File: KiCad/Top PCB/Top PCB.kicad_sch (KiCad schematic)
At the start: 44 parts, among them SW1 SW_MEC_5G, U1 SeeeduinoXIAO

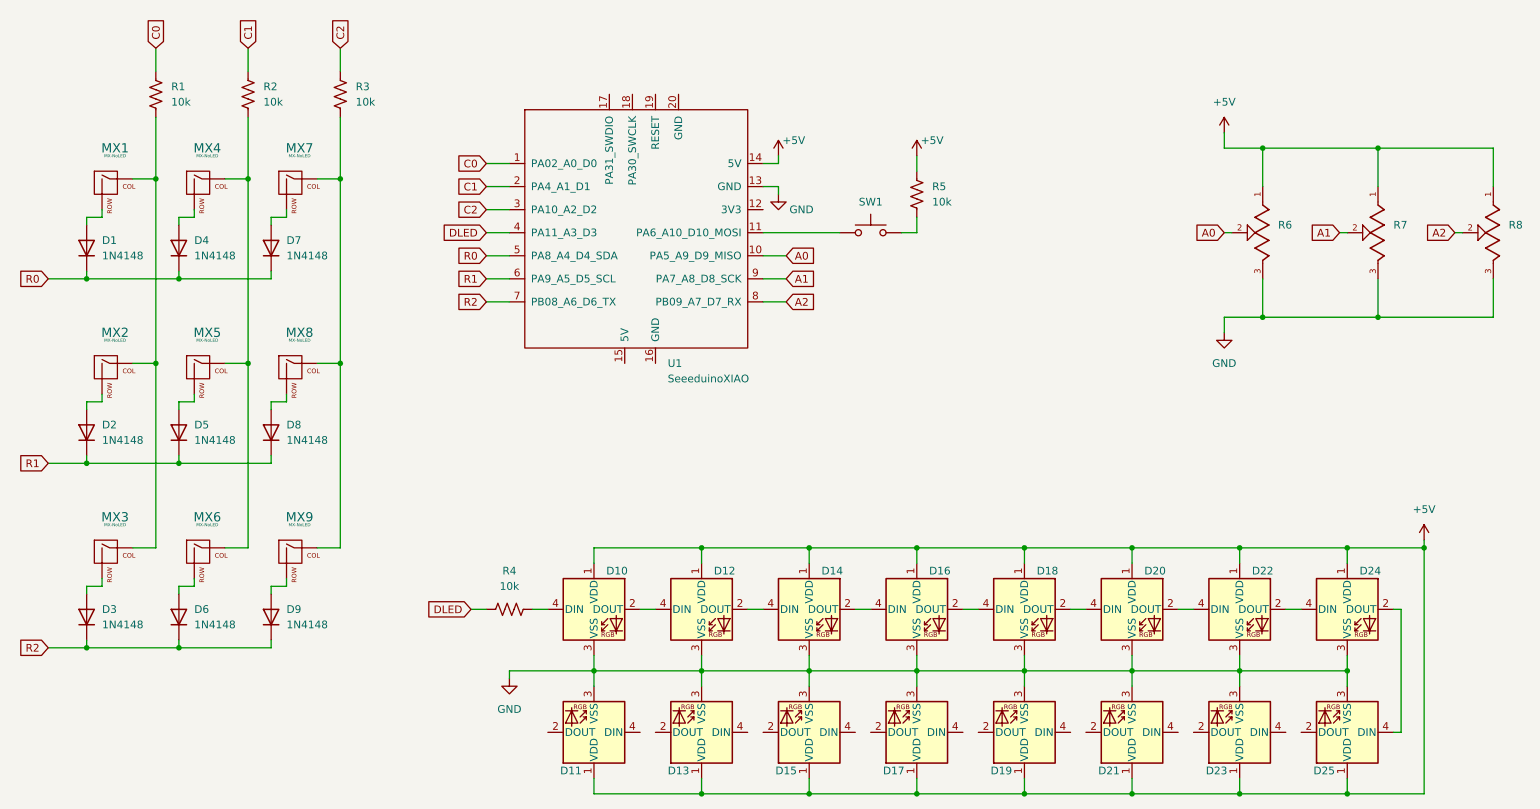
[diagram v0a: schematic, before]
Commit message: Split PCB into top, bottom. Develop Top
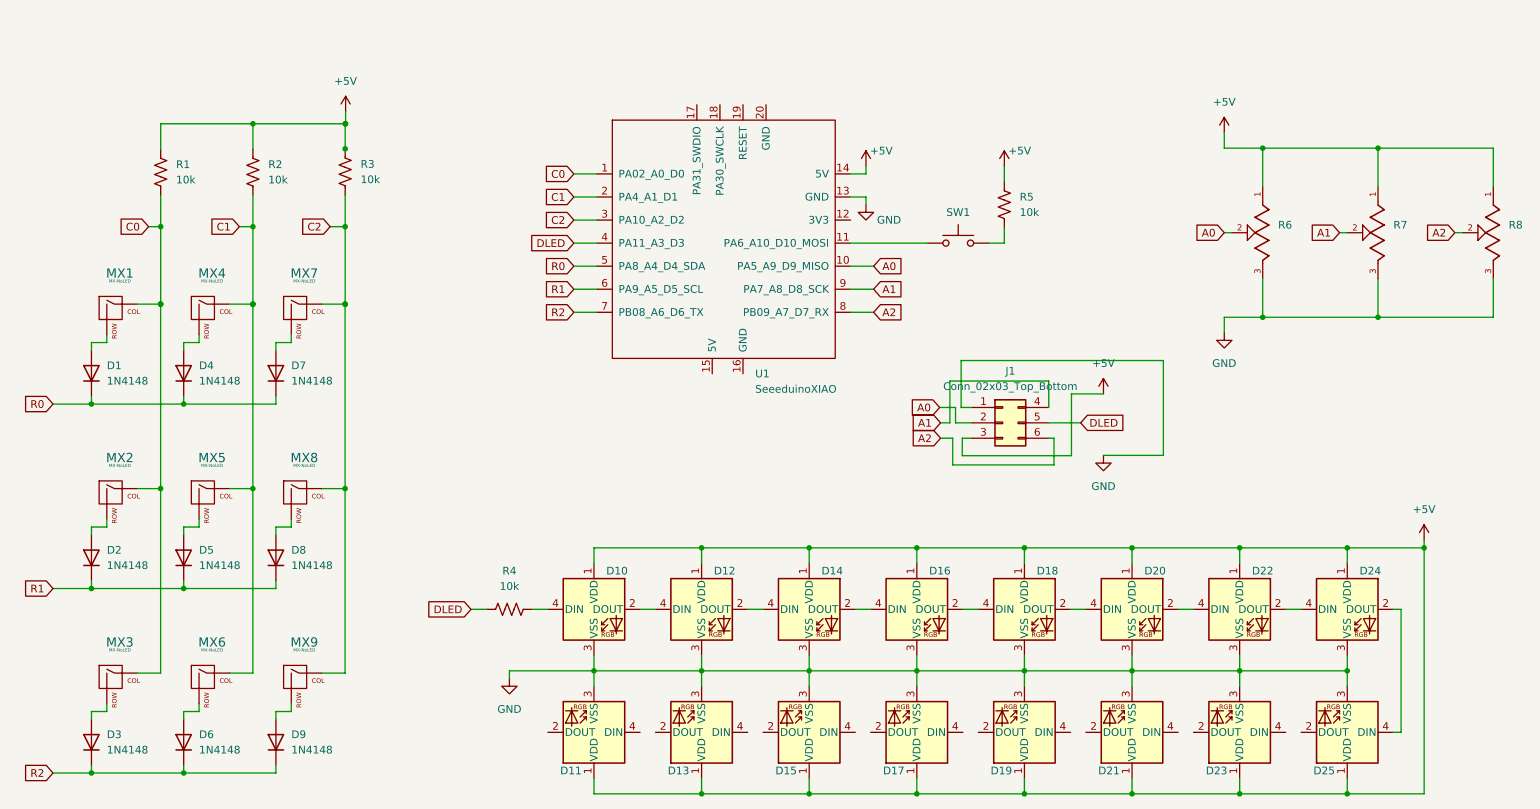
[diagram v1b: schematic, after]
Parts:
- added J1: Conn_02x03_Top_Bottom, Connector_PinHeader_2.54mm:PinHeader_2x03_P2.54mm_Vertical, symbol Connector_Generic:Conn_02x03_Top_Bottom
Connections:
- net +5V: now also R1.1, R2.1, R3.2, J1.3 (Pin_3)
- net A0: now also J1.2 (Pin_2)
- net A1: now also J1.4 (Pin_4)
- net A2: now also J1.6 (Pin_6)
- net C0: now also MX1.1 (COL), MX2.1 (COL), MX3.1 (COL), R1.2; no longer R1.1
- net C1: now also MX4.1 (COL), MX5.1 (COL), MX6.1 (COL), R2.2; no longer R2.1
- net C2: now also MX7.1 (COL), MX8.1 (COL), MX9.1 (COL)
- net DLED: now also J1.5 (Pin_5)
- net GND: now also J1.1 (Pin_1)
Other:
- moved on the sheet: D1, D2, D3, D4, D5, D6, D7, D8, D9, MX1, MX2, MX3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

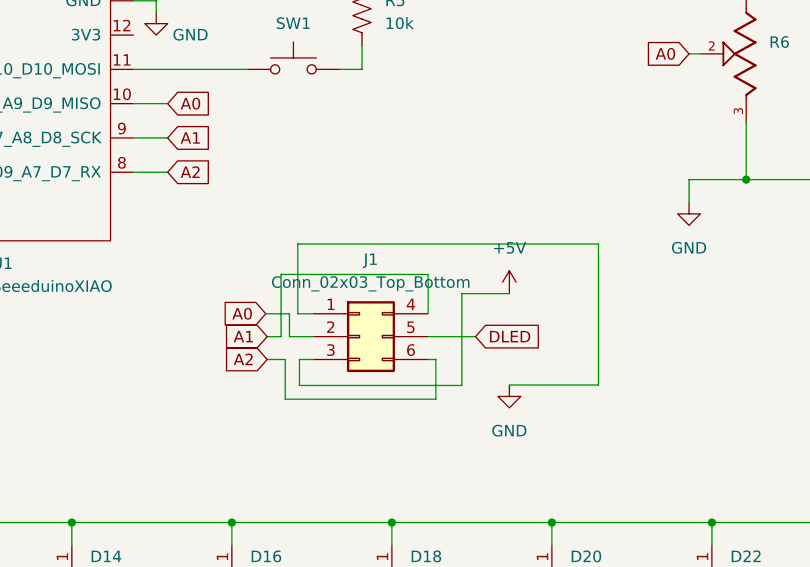
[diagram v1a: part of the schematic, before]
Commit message: Restructuring PCBs to only one top PCB, handwired switches
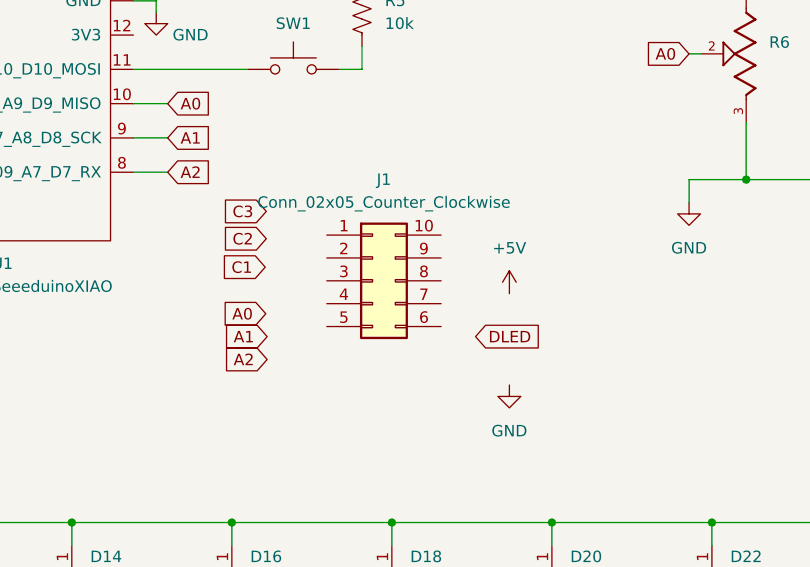
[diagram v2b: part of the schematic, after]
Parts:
- removed J1: Conn_02x03_Top_Bottom, Connector_PinHeader_2.54mm:PinHeader_2x03_P2.54mm_Vertical, symbol Connector_Generic:Conn_02x03_Top_Bottom
- added J1: Conn_02x05_Counter_Clockwise, Connector_PinHeader_2.54mm:PinHeader_2x05_P2.54mm_Vertical, symbol Connector_Generic:Conn_02x05_Counter_Clockwise
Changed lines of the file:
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@@
-    (stroke (width 0) (type default) (color 0 0 0 0))
-  )
-  (wire (pts (xy 178.6527 93.645) (xy 176.6431 93.645))
-    (stroke (width 0) (type default) (color 0 0 0 0))
-  )
-  (wire (pts (xy 213.4552 96.4802) (xy 213.4552 80.8131))
     (stroke (width 0) (type default) (color 0 0 0 0))
   )
@@
     (stroke (width 0) (type default) (color 0 0 0 0))
   )
-  (wire (pts (xy 194.5248 88.565) (xy 194.5248 84.1974))
-    (stroke (width 0) (type default) (color 0 0 0 0))
-  )
   (wire (pts (xy 226.06 132.08) (xy 226.06 134.62))
     (stroke (width 0) (type default) (color 0 0 0 0))
@@
     (stroke (width 0) (type default) (color 0 0 0 0))
   )
-  (wire (pts (xy 178.6527 98.0589) (xy 178.6527 93.645))
-    (stroke (width 0) (type default) (color 0 0 0 0))
-  )
   (wire (pts (xy 51.59 118.48) (xy 51.59 117.21))
     (stroke (width 0) (type default) (color 0 0 0 0))
@@
     (stroke (width 0) (type default) (color 0 0 0 0))
   )
-  (wire (pts (xy 203.5567 86.3311) (xy 198.2693 86.3311))
-    (stroke (width 0) (type default) (color 0 0 0 0))
-  )
   (wire (pts (xy 66.83 118.48) (xy 51.59 118.48))
     (stroke (width 0) (type default) (color 0 0 0 0))
@@
     (stroke (width 0) (type default) (color 0 0 0 0))
   )
-  (wire (pts (xy 203.5567 96.4802) (xy 213.4552 96.4802))
-    (stroke (width 0) (type default) (color 0 0 0 0))
-  )
-  (wire (pts (xy 195.3886 98.0589) (xy 178.6527 98.0589))
-    (stroke (width 0) (type default) (color 0 0 0 0))
-  )
   (wire (pts (xy 223.52 73.66) (xy 229.87 73.66))
     (stroke (width 0) (type default) (color 0 0 0 0))
@@
     (stroke (width 0) (type default) (color 0 0 0 0))
   )
-  (wire (pts (xy 194.5248 84.1974) (xy 178.1891 84.1974))
-    (stroke (width 0) (type default) (color 0 0 0 0))
-  )
-  (wire (pts (xy 195.3886 93.645) (xy 195.3886 98.0589))
-    (stroke (width 0) (type default) (color 0 0 0 0))
-  )
-  (wire (pts (xy 194.5248 91.105) (xy 199.7978 91.105))
-    (stroke (width 0) (type default) (color 0 0 0 0))
-  )
   (wire (pts (xy 208.28 132.08) (xy 226.06 132.08))
     (stroke (width 0) (type default) (color 0 0 0 0))
@@
     (stroke (width 0) (type default) (color 0 0 0 0))
   )
-  (wire (pts (xy 213.4552 80.8131) (xy 180.0435 80.8131))
-    (stroke (width 0) (type default) (color 0 0 0 0))
-  )
   (wire (pts (xy 119.38 152.4) (xy 137.16 152.4))
     (stroke (width 0) (type default) (color 0 0 0 0))
@@
     (stroke (width 0) (type default) (color 0 0 0 0))
   )
-  (wire (pts (xy 176.4927 88.565) (xy 179.1213 88.565))
-    (stroke (width 0) (type default) (color 0 0 0 0))
-  )
   (wire (pts (xy 51.59 148.96) (xy 36.35 148.96))
     (stroke (width 0) (type default) (color 0 0 0 0))
@@
     (stroke (width 0) (type default) (color 0 0 0 0))
   )
-  (wire (pts (xy 181.8248 88.565) (xy 180.0435 88.565))
-    (stroke (width 0) (type default) (color 0 0 0 0))
-  )
   (wire (pts (xy 187.18 48.71) (xy 187.18 51.25))
     (stroke (width 0) (type default) (color 0 0 0 0))
@@
     (stroke (width 0) (type default) (color 0 0 0 0))
   )
-  (wire (pts (xy 178.1891 84.1974) (xy 178.1891 91.105))
-    (stroke (width 0) (type default) (color 0 0 0 0))
-  )
   (wire (pts (xy 229.87 67.31) (xy 229.87 73.66))
     (stroke (width 0) (type default) (color 0 0 0 0))
   )
-  (wire (pts (xy 194.5248 93.645) (xy 195.3886 93.645))
-    (stroke (width 0) (type default) (color 0 0 0 0))
-  )
   (wire (pts (xy 45.79 58.69) (xy 47.79 58.69))
     (stroke (width 0) (type default) (color 0 0 0 0))
@@
     (stroke (width 0) (type default) (color 0 0 0 0))
   )
-  (wire (pts (xy 180.0435 88.565) (xy 180.0435 80.8131))
-    (stroke (width 0) (type default) (color 0 0 0 0))
-  )
   (wire (pts (xy 30 88) (xy 36.35 88))
     (stroke (width 0) (type default) (color 0 0 0 0))
@@
     (stroke (width 0) (type default) (color 0 0 0 0))
   )
-  (wire (pts (xy 198.2693 96.529) (xy 180.229 96.529))
-    (stroke (width 0) (type default) (color 0 0 0 0))
-  )
   (wire (pts (xy 59.21 132.45) (xy 63.02 132.45))
     (stroke (width 0) (type default) (color 0 0 0 0))
@@
     (stroke (width 0) (type default) (color 0 0 0 0))
   )
-  (wire (pts (xy 179.1213 88.565) (xy 179.1213 91.105))
-    (stroke (width 0) (type default) (color 0 0 0 0))
-  )
   (wire (pts (xy 78.27 41.69) (xy 63.03 41.69))
     (stroke (width 0) (type default) (color 0 0 0 0))
@@
     (stroke (width 0) (type default) (color 0 0 0 0))
   )
-  (wire (pts (xy 181.8248 93.645) (xy 180.229 93.645))
-    (stroke (width 0) (type default) (color 0 0 0 0))
-  )
-  (wire (pts (xy 178.1891 91.105) (xy 176.6431 91.105))
-    (stroke (width 0) (type default) (color 0 0 0 0))
-  )
   (wire (pts (xy 105.41 132.08) (xy 105.41 133.35))
     (stroke (width 0) (type default) (color 0 0 0 0))
@@
     (stroke (width 0) (type default) (color 0 0 0 0))
   )
-  (wire (pts (xy 180.229 93.645) (xy 180.229 96.529))
-    (stroke (width 0) (type default) (color 0 0 0 0))
-  )
   (wire (pts (xy 172.72 111.76) (xy 190.5 111.76))
     (stroke (width 0) (type default) (color 0 0 0 0))
@@
     (stroke (width 0) (type default) (color 0 0 0 0))
   )
-  (wire (pts (xy 198.2693 86.3311) (xy 198.2693 96.529))
-    (stroke (width 0) (type default) (color 0 0 0 0))
-  )
   (wire (pts (xy 51.59 88) (xy 51.59 86.73))
-    (stroke (width 0) (type default) (color 0 0 0 0))
-  )
-  (wire (pts (xy 179.1213 91.105) (xy 181.8248 91.105))
     (stroke (width 0) (type default) (color 0 0 0 0))
   )
@@
     )
   )
+  (global_label "C1" (shape input) (at 176.4301 83.3848 180) (fields_autoplaced)
+    (effects (font (size 1.27 1.27)) (justify right))
+    (property "Intersheet References" "${INTERSHEET_REFS}" (id 0) (at 171.5375 83.3054 0)
+      (effects (font (size 1.27 1.27)) (justify right) hide)
+    )
+  )
   (global_label "DLED" (shape input) (at 199.7978 91.105 0) (fields_autoplaced)
     (effects (font (size 1.27 1.27)) (justify left))
@@
     )
   )
+  (global_label "C2" (shape input) (at 176.547 80.2297 180) (fields_autoplaced)
+    (effects (font (size 1.27 1.27)) (justify right))
+    (property "Intersheet References" "${INTERSHEET_REFS}" (id 0) (at 171.6544 80.1503 0)
+      (effects (font (size 1.27 1.27)) (justify right) hide)
+    )
+  )
   (global_label "A2" (shape input) (at 261.62 59.69 180) (fields_autoplaced)
     (effects (font (size 1.27 1.27)) (justify right))
@@
     (effects (font (size 1.27 1.27)) (justify right))
     (property "Intersheet References" "${INTERSHEET_REFS}" (id 0) (at 171.9319 91.0256 0)
+      (effects (font (size 1.27 1.27)) (justify right) hide)
+    )
+  )
+  (global_label "C3" (shape input) (at 176.547 77.1914 180) (fields_autoplaced)
+    (effects (font (size 1.27 1.27)) (justify right))
+    (property "Intersheet References" "${INTERSHEET_REFS}" (id 0) (at 171.6544 77.112 0)
       (effects (font (size 1.27 1.27)) (justify right) hide)
     )
@@
     (pin "9")
   )
+  (symbol (lib_id "Connector_Generic:Conn_02x05_Counter_Clockwise") (at 188.3496 84.904 0) (unit 1)
+    (in_bom yes) (on_board yes) (fields_autoplaced)
+    (property "Reference" "J1" (id 0) (at 189.6196 73.66 0))
+    (property "Value" "Conn_02x05_Counter_Clockwise" (id 1) (at 189.6196 76.2 0))
+    (property "Footprint" "Connector_PinHeader_2.54mm:PinHeader_2x05_P2.54mm_Vertical" (id 2) (at 188.3496 84.904 0)
+      (effects (font (size 1.27 1.27)) hide)
+    )
+    (property "Datasheet" "~" (id 3) (at 188.3496 84.904 0)
+      (effects (font (size 1.27 1.27)) hide)
+    )
+    (pin "1")
+    (pin "10")
+    (pin "2")
+    (pin "3")
+    (pin "4")
+    (pin "5")
+    (pin "6")
+    (pin "7")
+    (pin "8")
+    (pin "9")
+  )
   (symbol (lib_id "Diode:1N4148") (at 36.35 143.88 90) (unit 1)
     (in_bom yes) (on_board yes) (fields_autoplaced)
@@
     (pin "2")
   )
-  (symbol (lib_id "Connector_Generic:Conn_02x03_Top_Bottom") (at 186.9048 91.105 0) (unit 1)
-    (in_bom yes) (on_board yes) (fields_autoplaced)
-    (property "Reference" "J1" (id 0) (at 188.1748 82.55 0))
-    (property "Value" "Conn_02x03_Top_Bottom" (id 1) (at 188.1748 85.09 0))
-    (property "Footprint" "Connector_PinHeader_2.54mm:PinHeader_2x03_P2.54mm_Vertical" (id 2) (at 186.9048 91.105 0)
-      (effects (font (size 1.27 1.27)) hide)
-    )
-    (property "Datasheet" "~" (id 3) (at 186.9048 91.105 0)
-      (effects (font (size 1.27 1.27)) hide)
-    )
-    (pin "1")
-    (pin "2")
-    (pin "3")
-    (pin "4")
-    (pin "5")
-    (pin "6")
-  )
   (symbol (lib_id "MX_Alps_Hybrid:MX-NoLED") (at 40.16 72.76 0) (unit 1)
     (in_bom yes) (on_board yes) (fields_autoplaced)
@@
       (reference "D25") (unit 1) (value "WS2812B") (footprint "LED_SMD:LED_WS2812B_PLCC4_5.0x5.0mm_P3.2mm")
     )
-    (path "/c561bd86-e169-4f35-84fd-77fdf95e857b"
-      (reference "J1") (unit 1) (value "Conn_02x03_Top_Bottom") (footprint "Connector_PinHeader_2.54mm:PinHeader_2x03_P2.54mm_Vertical")
+    (path "/0dfddbe2-cd33-467a-bbc9-cff1c1af8c23"
+      (reference "J1") (unit 1) (value "Conn_02x05_Counter_Clockwise") (footprint "Connector_PinHeader_2.54mm:PinHeader_2x05_P2.54mm_Vertical")
     )
     (path "/cd9b38e3-ea2b-4303-9425-19d1dfcc07ff"
